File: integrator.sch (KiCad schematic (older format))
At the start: 21 parts, among them J1 SJ-3524-SMT, J2 SJ-3524-SMT, SW1 EVQP40B3M, SW2 EVQP40B3M, SW3 SW_Push_LED, U1 Teensy3.2, U2 ICM-42605

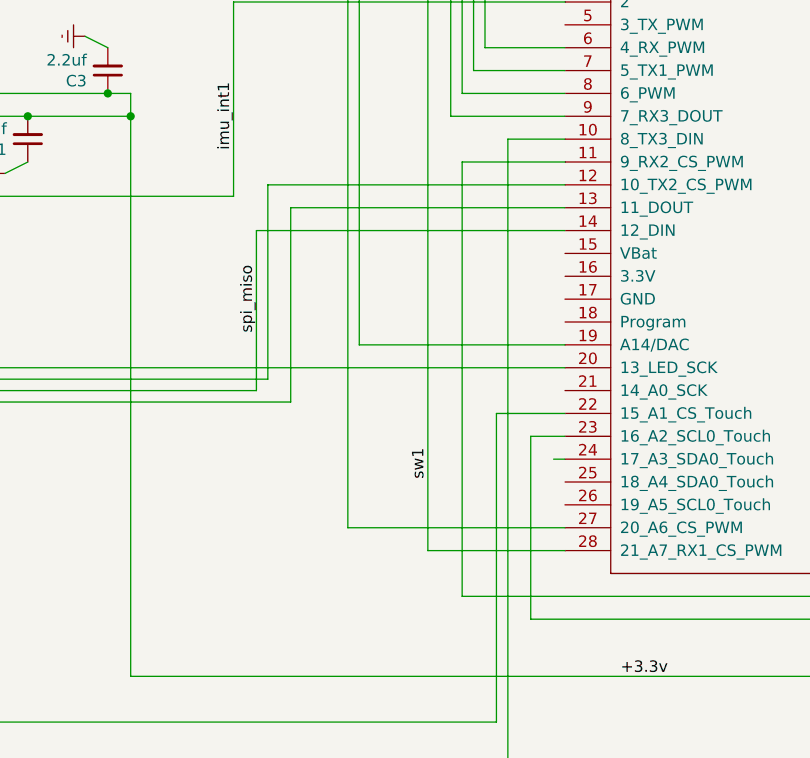
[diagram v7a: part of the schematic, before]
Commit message: moved po_wake to analog pin 14 +tweaks
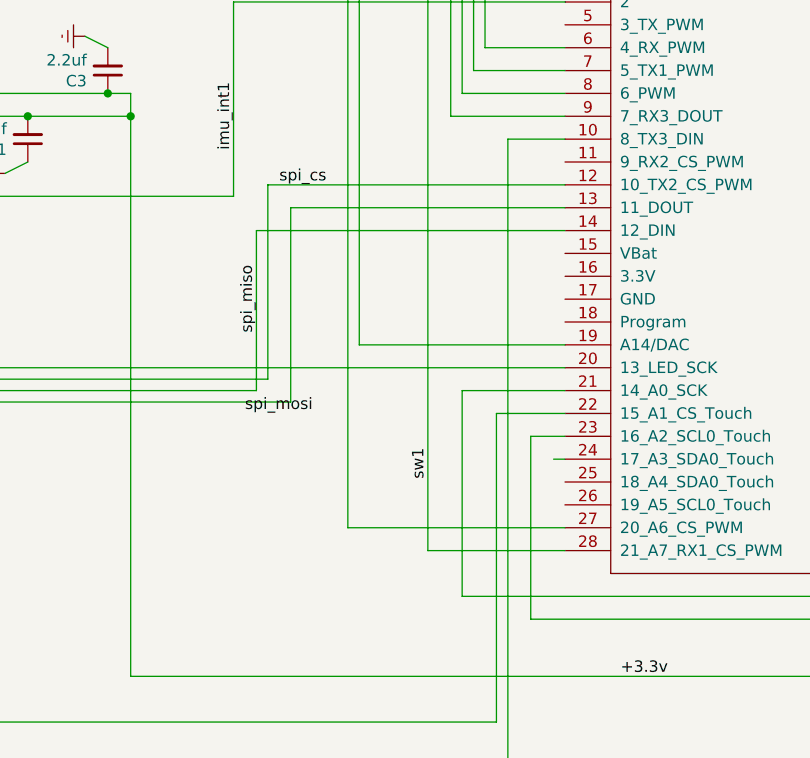
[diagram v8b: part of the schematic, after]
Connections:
- net po_wake: now also U1.21 (14_A0_SCK); no longer U1.11 (9_RX2_CS_PWM)
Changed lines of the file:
@@
 	5450 2700 2350 2700
-Wire Wire Line
-	6050 4450 5600 4450
-Wire Wire Line
-	5600 4450 5600 6350
 Wire Wire Line
 	4150 6700 8150 6700
@@
 Text Label 2950 7600 2    50   ~ 0
 led2
+Text Label 4800 4550 0    50   ~ 0
+spi_cs
+Text Label 4650 5550 0    50   ~ 0
+spi_mosi
+Wire Wire Line
+	6050 5450 5600 5450
+Wire Wire Line
+	5600 5450 5600 6350
 $EndSCHEMATC
